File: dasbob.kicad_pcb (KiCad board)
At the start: 2 copper layers, 243.5 x 104.8 mm, 68 parts, among them J1 TRRS LEFT, J2 TRRS LEFT, SW1 SW_Push, SW10 SW_Push, SW11 SW_Push, SW12 SW_Push, SW13 SW_Push, SW14 SW_Push, SW15 SW_Push, SW16 SW_Push, SW17 SW_Push, SW18 SW_Push, SW19 SW_Push, SW2 SW_Push, SW20 SW_Push, SW21 SW_Push, SW22 SW_Push, SW23 SW_Push, SW24 SW_Push, SW25 SW_Push, SW26 SW_Push, SW27 SW_Push, SW28 SW_Push, SW29 SW_Push, SW3 SW_Push, SW30 SW_Push, SW31 SW_Push, SW32 SW_Push, SW33 SW_Push, SW34 SW_Push, SW35 SW_Push, SW36 SW_Push, SW4 SW_Push, SW5 SW_Push, SW6 SW_Push, SW7 SW_Push, SW8 SW_Push, SW9 SW_Push, U1 Elite-C RIGHT, U2 Elite-C LEFT, U3 OLED1, U4 OLED2

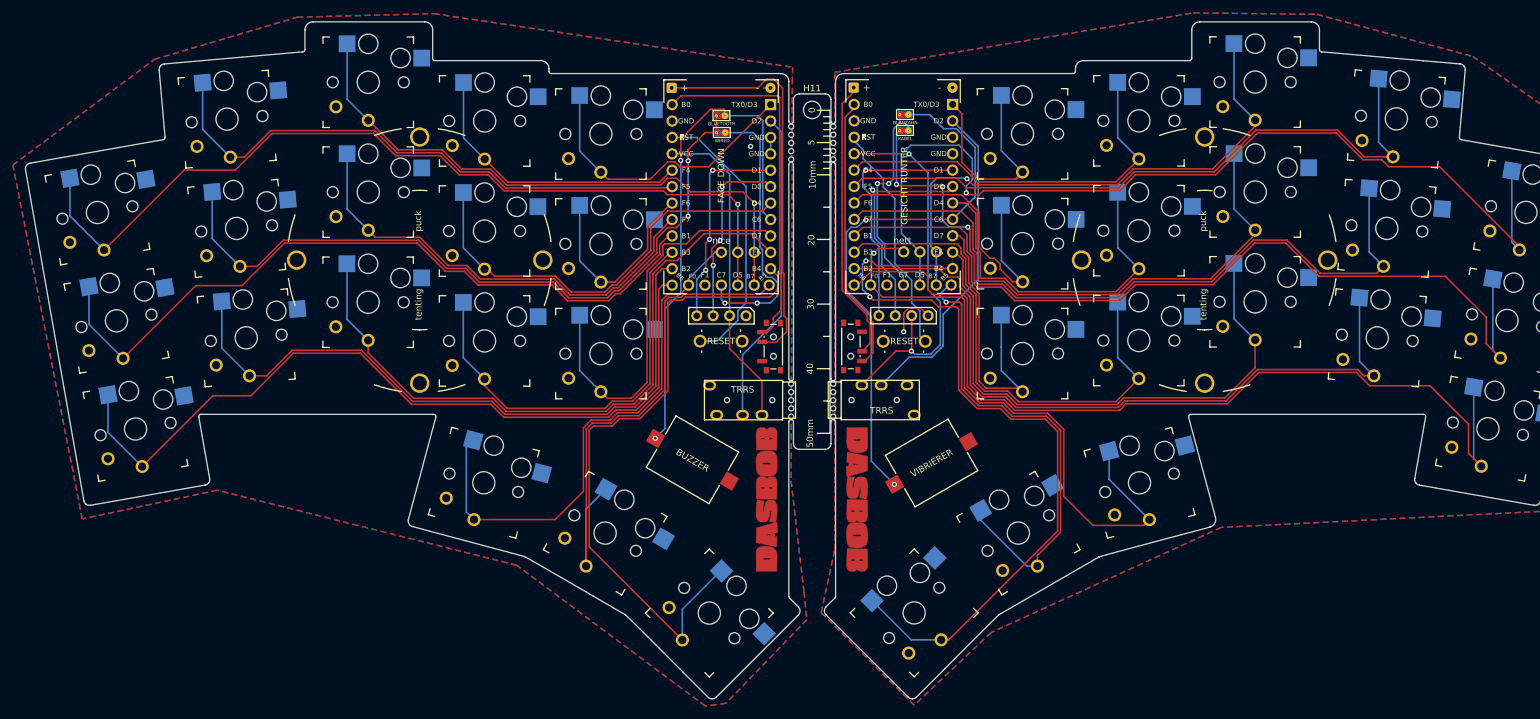
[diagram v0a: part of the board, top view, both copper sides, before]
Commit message: thicken power lines
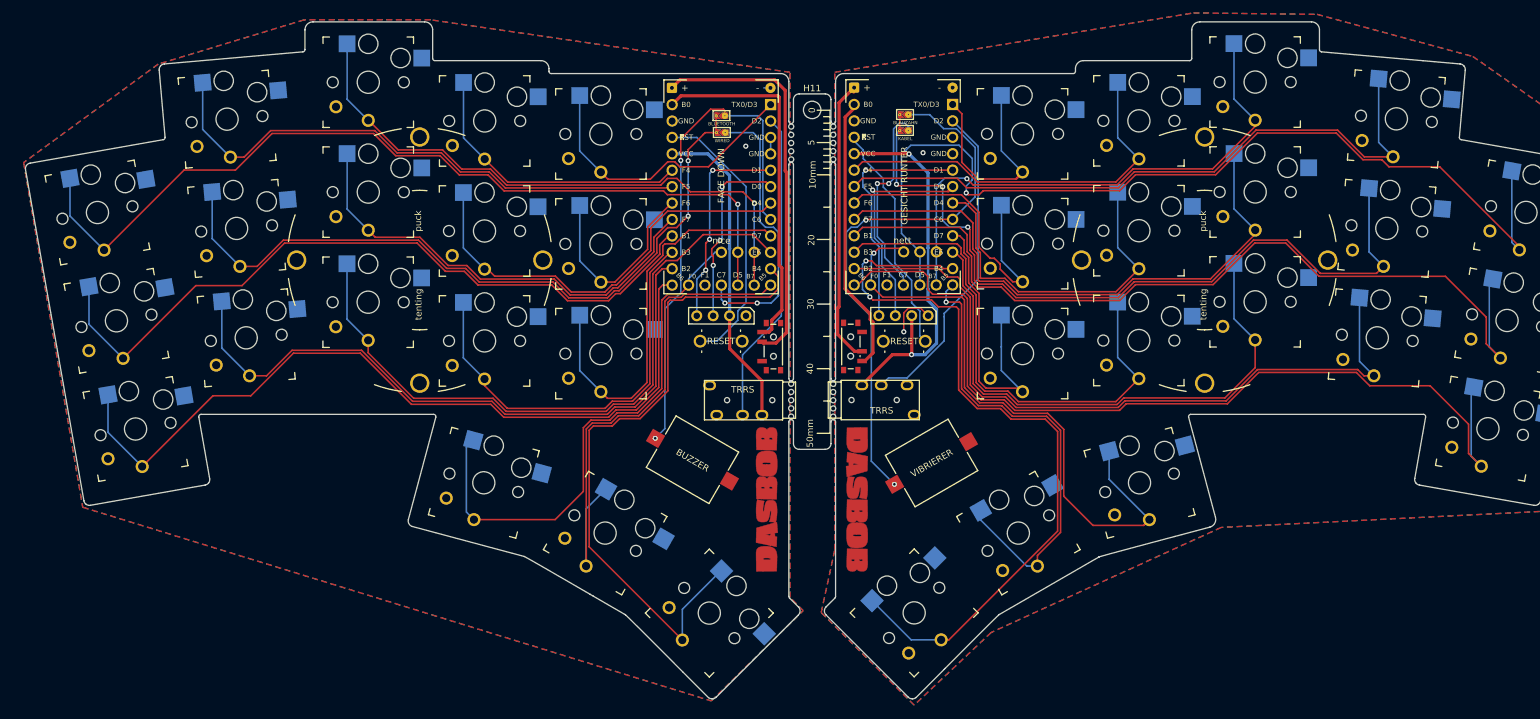
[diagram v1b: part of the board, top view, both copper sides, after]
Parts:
- moved TAB1 0.07 mm to (159.5, 36.9)
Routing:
- net 3a: track 84.9 -> 83.5 mm
- net TAB: track 43.8 -> 44.8 mm
- net CVV: track 60.7 -> 59.9 mm
- net 17a: track 73.0 -> 72.4 mm
- net 6a: track 135.3 -> 135.8 mm
- net DNG: vias 1 -> 2

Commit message: Some minor changes
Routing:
- net C7: track 43.6 -> 34.6 mm
- net DNG: track 7.50 -> 0.00 mm
- net CVV: track 59.9 -> 57.9 mm, vias 2 -> 3
- net 1P: track 37.2 -> 35.2 mm
- net 2P: track 34.8 -> 32.8 mm
- net 7a: track 120.3 -> 118.8 mm
- net TSR: track 35.5 -> 36.1 mm
